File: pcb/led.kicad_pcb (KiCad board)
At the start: 2 copper layers, 53.3 x 24.1 mm, 12 parts, among them J1 CONN_01X03, J2 CONN_01X03, J3 CONN_01X04, U1 DSN-MINI-360, U2 4504, U3 4504

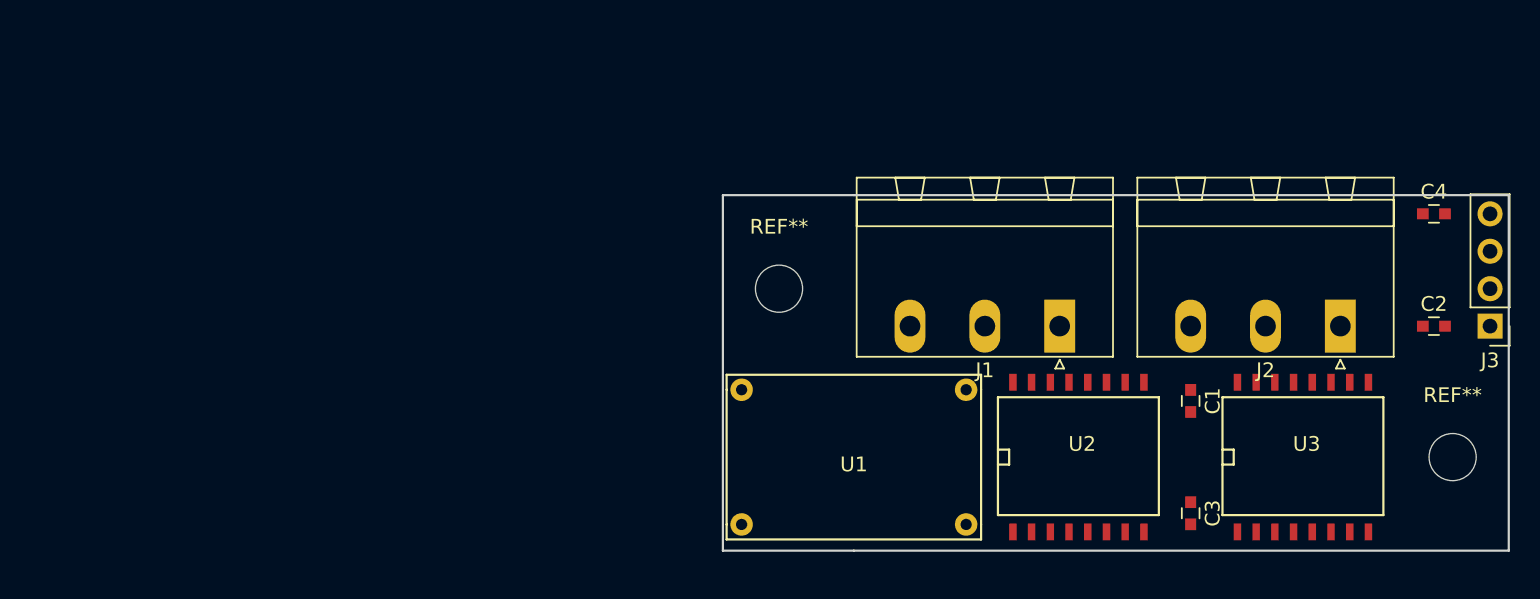
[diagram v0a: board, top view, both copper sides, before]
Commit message: Add measurements; update schematic.
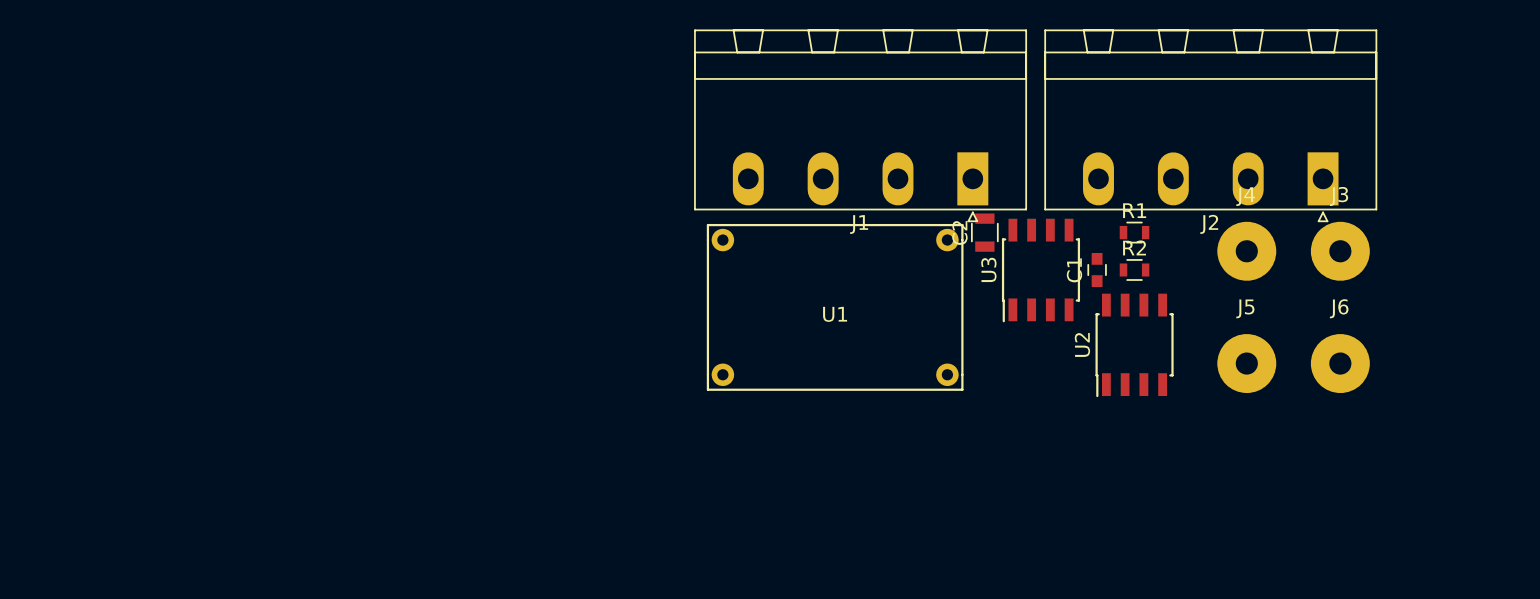
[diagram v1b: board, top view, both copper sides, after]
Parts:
- removed C3, C4: C, Capacitors_SMD:C_0603
- removed REF** (x2): MountingHole_3.2mm_M3, Mounting_Holes:MountingHole_3.2mm_M3
- added J4: CONN_01X01, Wire_Pads:SolderWirePad_single_1-5mmDrill, F.Cu at (188.0, 105.4)
- added J5: CONN_01X01, Wire_Pads:SolderWirePad_single_1-5mmDrill, F.Cu at (188.0, 113.0)
- added J6: CONN_01X01, Wire_Pads:SolderWirePad_single_1-5mmDrill, F.Cu at (194.3, 113.0)
- added R1: 120R, Resistors_SMD:R_0603, F.Cu at (180.3, 104.1)
- added R2: 120R, Resistors_SMD:R_0603, F.Cu at (180.3, 106.7)
- C1: value C -> 100n
- C2: value C -> 1u; footprint Capacitors_SMD:C_0603 -> Resistors_SMD:R_0805
- J1, J2: value CONN_01X03 -> CONN_01X04; footprint Connectors_Phoenix:PhoenixContact_MSTBA-G_03x5.08mm_Angled -> Connectors_Phoenix:PhoenixContact_MSTBA-G_04x5.08mm_Angled
- J3: value CONN_01X04 -> CONN_01X01; footprint Pin_Headers:Pin_Header_Straight_1x04_Pitch2.54mm -> Wire_Pads:SolderWirePad_single_1-5mmDrill
- U2, U3: value 4504 -> MAX485; footprint SMD_Packages:SO-16-W -> Housings_SOIC:SOIC-8_3.9x4.9mm_Pitch1.27mm
- moved C2 31.1 mm to (170.2, 104.1), turned to 90 degrees
- moved U3 21.8 mm to (174.0, 106.7), turned to 90 degrees
- moved J1 11.6 mm to (169.4, 100.5)
- moved J3 11.4 mm to (194.3, 105.4), turned to 0 degrees
- moved C1 10.9 mm to (177.8, 106.7), turned to 90 degrees
- moved U1 10.2 mm to (160.0, 109.2)
- moved J2 10.1 mm to (193.1, 100.5)
- moved U2 8.52 mm to (180.3, 111.8), turned to 90 degrees
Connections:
- C1 pad 1: +12V -> (no net)
- C2 pad 1: +5V -> GND
- C2 pad 2: GND -> +12V
- J1 pad 3: +12V -> Net-(J1-Pad3)
- J2 pad 3: +12V -> Net-(J2-Pad3)
- U1 pad IN+: +12V -> (no net)
- U1 pad IN-: GND -> (no net)
- U1 pad OUT-: GND -> (no net)
- U2 pad 1: +12V -> Net-(J4-Pad1)
- U2 pad 2: Net-(J3-Pad2) -> GND
- U2 pad 3: Net-(J1-Pad2) -> GND
- U2 pad 4: Net-(U2-Pad4) -> (no net)
- U2 pad 6: Net-(U2-Pad6) -> Net-(J1-Pad2)
- U2 pad 7: GND -> Net-(J1-Pad3)
- U2 pad 8: GND -> +5V
- U3 pad 1: +5V -> (no net)
- U3 pad 2: Net-(J2-Pad2) -> +5V
- U3 pad 3: Net-(J3-Pad3) -> +5V
- U3 pad 6: Net-(U3-Pad6) -> Net-(J2-Pad2)
- U3 pad 7: GND -> Net-(J2-Pad3)
- U3 pad 8: GND -> +5V
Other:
- board outline removed

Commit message: Fix errors.
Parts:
- added MK1: Mounting_Hole, Mounting_Holes:MountingHole_3.5mm, F.Cu at (128.3, 103.5)
- added R3: 120R, Resistors_SMD:R_0603, F.Cu at (133.3, 111.8)
- C2: footprint Resistors_SMD:R_0805 -> Capacitors_SMD:C_0805
- R1, R2: value 120R -> 270R
- moved J2 63.2 mm to (132.1, 116.8), turned to 0 degrees
- moved J1 62.3 mm to (109.2, 116.8), turned to 0 degrees
- moved J3 59.1 mm to (135.3, 102.9)
- moved R2 56.3 mm to (124.5, 113.7), turned to 180 degrees
- moved U2 52.1 mm to (128.3, 110.5), turned to 0 degrees
- moved J4 48.3 mm to (139.7, 102.9)
- moved C2 47.7 mm to (122.6, 102.2), turned to 180 degrees
- moved R1 47.3 mm to (133.3, 109.2), turned to 270 degrees
- moved J6 46.8 mm to (148.6, 102.9)
- moved U1 45.7 mm to (114.3, 109.2), turned to 180 degrees
- moved J5 45.0 mm to (144.1, 102.9)
- moved C1 43.1 mm to (135.3, 113.7), turned to 180 degrees
- moved U3 32.8 mm to (141.6, 111.8), turned to 0 degrees
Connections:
- C1 pad 1: (no net) -> +5V
- J1 pad 1: GND -> +12V
- J1 pad 4: +12V -> GND
- J2 pad 1: GND -> +12V
- J2 pad 4: +12V -> GND
- R1 pad 1: Net-(J1-Pad3) -> +5V
- R1 pad 2: GND -> Net-(J1-Pad2)
- U1 pad IN+: (no net) -> +12V
- U1 pad IN-: (no net) -> GND
- U1 pad OUT+: (no net) -> +5V
- U1 pad OUT-: (no net) -> GND
- U2 pad 6: Net-(J1-Pad2) -> Net-(J1-Pad3)
- U2 pad 7: Net-(J1-Pad3) -> Net-(J1-Pad2)
- U3 pad 6: Net-(J2-Pad2) -> Net-(J2-Pad3)
- U3 pad 7: Net-(J2-Pad3) -> Net-(J2-Pad2)

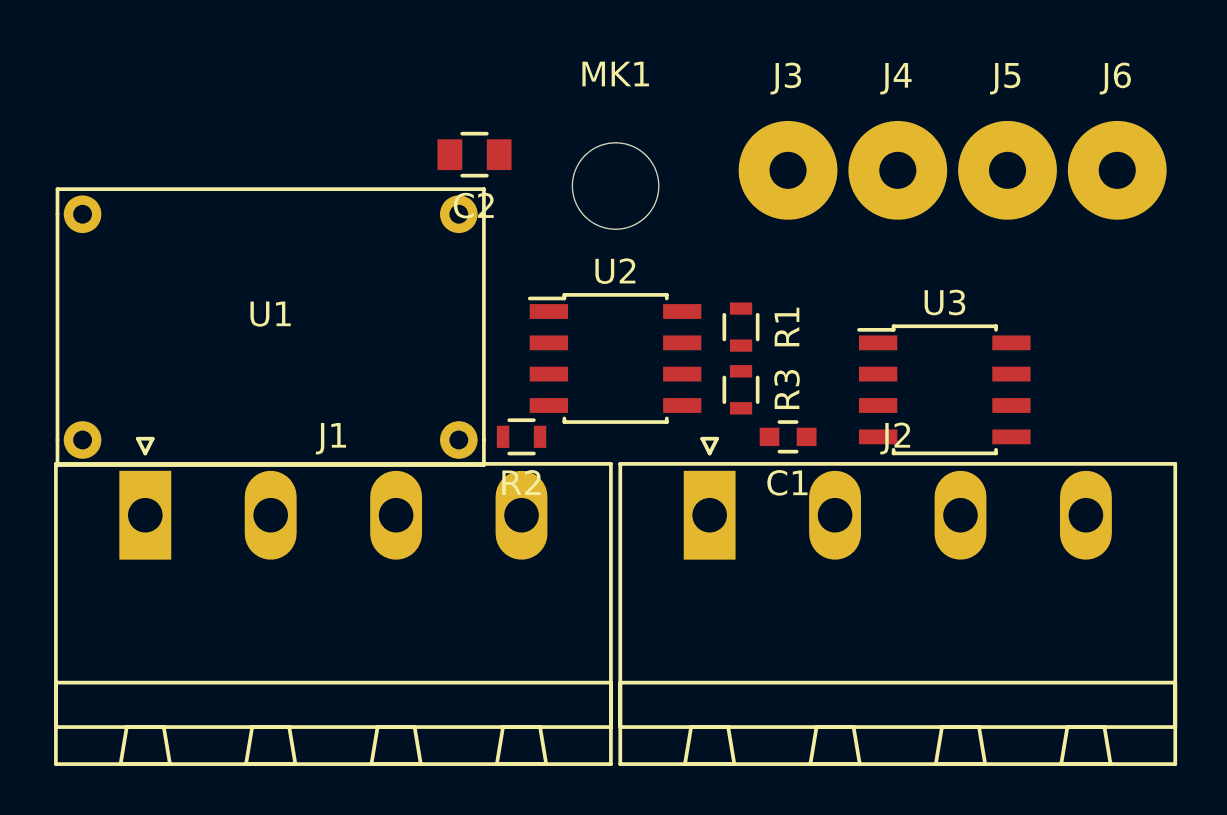
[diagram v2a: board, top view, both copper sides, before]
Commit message: Change to 3.5 mm pitch connectors. Finalize PCB layout.
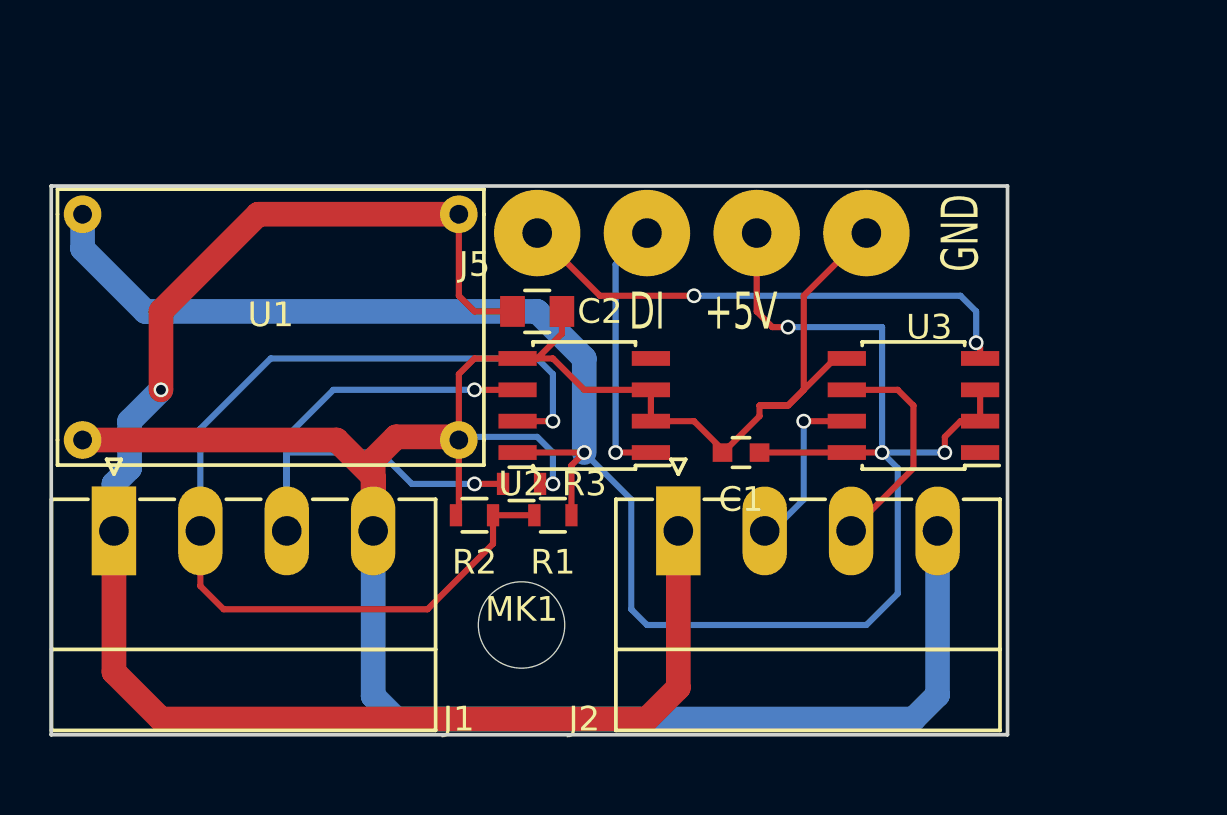
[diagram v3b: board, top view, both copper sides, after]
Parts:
- J1, J2: footprint Connectors_Phoenix:PhoenixContact_MSTBA-G_04x5.08mm_Angled -> Connectors_Phoenix:PhoenixContact_MC-G_04x3.50mm_Angled
- J3, J4, J5, J6: footprint Wire_Pads:SolderWirePad_single_1-5mmDrill -> Wire_Pads:SolderWirePad_single_1-2mmDrill
- moved J5 19.2 mm to (125.1, 105.4)
- moved MK1 18.2 mm to (124.5, 121.3)
- moved R1 10.8 mm to (125.7, 116.8), turned to 180 degrees
- moved J4 10.5 mm to (129.5, 105.4)
- moved J6 10.5 mm to (138.4, 105.4)
- moved R3 9.67 mm to (124.5, 115.6), turned to 0 degrees
- moved C2 6.84 mm to (125.1, 108.6)
- moved R2 3.70 mm to (122.6, 116.8)
- moved J3 2.84 mm to (134.0, 105.4)
- moved U2 2.29 mm to (127.0, 112.4), turned to 180 degrees
- moved C1 2.01 mm to (133.3, 114.3)
- moved J2 1.42 mm to (130.8, 117.5)
- moved J1 1.42 mm to (108.0, 117.5)
- moved U3 1.42 mm to (140.3, 112.4), turned to 180 degrees
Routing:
- net GND: track 0.00 -> 103.7 mm, vias 0 -> 1
- net +5V: track 0.00 -> 82.2 mm, vias 0 -> 4
- net +12V: track 0.00 -> 65.4 mm, vias 0 -> 1
- net Net-(J1-Pad2): track 0.00 -> 41.6 mm, vias 0 -> 1
- net Net-(J1-Pad3): track 0.00 -> 26.9 mm, vias 0 -> 2
- net Net-(J5-Pad1): track 0.00 -> 21.1 mm, vias 0 -> 2
- net Net-(J4-Pad1): track 0.00 -> 10.8 mm, vias 0 -> 1
- net Net-(J2-Pad3): track 0.00 -> 9.99 mm
- net Net-(J2-Pad2): track 0.00 -> 7.03 mm, vias 0 -> 1
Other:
- board outline added: 38.7 x 22.2 mm
- board text added: "+5V"
- board text added: "DI"
- board text added: "GND"
- board text added: "Sommerhack 2017"

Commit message: Adjust layout.
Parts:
- moved J5 17.1 mm to (142.2, 105.7)
- moved J6 4.33 mm to (134.1, 105.7)
- moved J3 4.20 mm to (138.2, 105.7)
- moved C1 1.27 mm to (134.6, 114.3)
- moved U2 1.27 mm to (128.3, 112.4)
- moved J4 0.57 mm to (130.0, 105.7)
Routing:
- net Net-(J5-Pad1): track 21.1 -> 5.16 mm, vias 2 -> 0
- net GND: track 103.7 -> 118.5 mm
- net +5V: track 82.2 -> 67.5 mm, vias 4 -> 3
- net Net-(J1-Pad2): track 41.6 -> 28.1 mm, vias 1 -> 2
- net Net-(J1-Pad3): track 26.9 -> 17.8 mm, vias 2 -> 1
- net Net-(J4-Pad1): track 10.8 -> 11.3 mm, vias 1 -> 2
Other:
- board text added: "DO"

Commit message: Fix label.
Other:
- board text added: "+12V"
- board text removed: "+5V"
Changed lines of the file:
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@@
   )
   (setup
-    (last_trace_width 0.5)
+    (last_trace_width 0.25)
     (user_trace_width 0.5)
     (user_trace_width 1)
@@
     (effects (font (size 1.5 1) (thickness 0.2)))
   )
-  (gr_text +5V (at 137.668 108.585) (layer F.SilkS)
+  (gr_text +12V (at 137.668 108.585) (layer F.SilkS)
     (effects (font (size 1.5 1) (thickness 0.2)))
   )

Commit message: Add ESP code.
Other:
- rule pad_to_mask_clearance: 0.2 -> -0.3
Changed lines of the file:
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@@
     (pad_size 1.524 1.524)
     (pad_drill 0.762)
-    (pad_to_mask_clearance 0.2)
+    (pad_to_mask_clearance -0.3)
+    (pad_to_paste_clearance -0.22)
     (aux_axis_origin 0 0)
     (visible_elements FFFFF77F)
     (pcbplotparams
-      (layerselection 0x00030_80000001)
+      (layerselection 0x0d0fc_80000001)
       (usegerberextensions false)
       (excludeedgelayer true)
@@
       (padsonsilk false)
       (subtractmaskfromsilk false)
-      (outputformat 1)
+      (outputformat 5)
       (mirror false)
-      (drillshape 1)
+      (drillshape 0)
       (scaleselection 1)
-      (outputdirectory ""))
+      (outputdirectory gerber/))
   )
   (net 0 "")
